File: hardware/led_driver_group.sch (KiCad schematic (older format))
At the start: 26 parts, among them U4 TLC6C5912GQPWRQ1

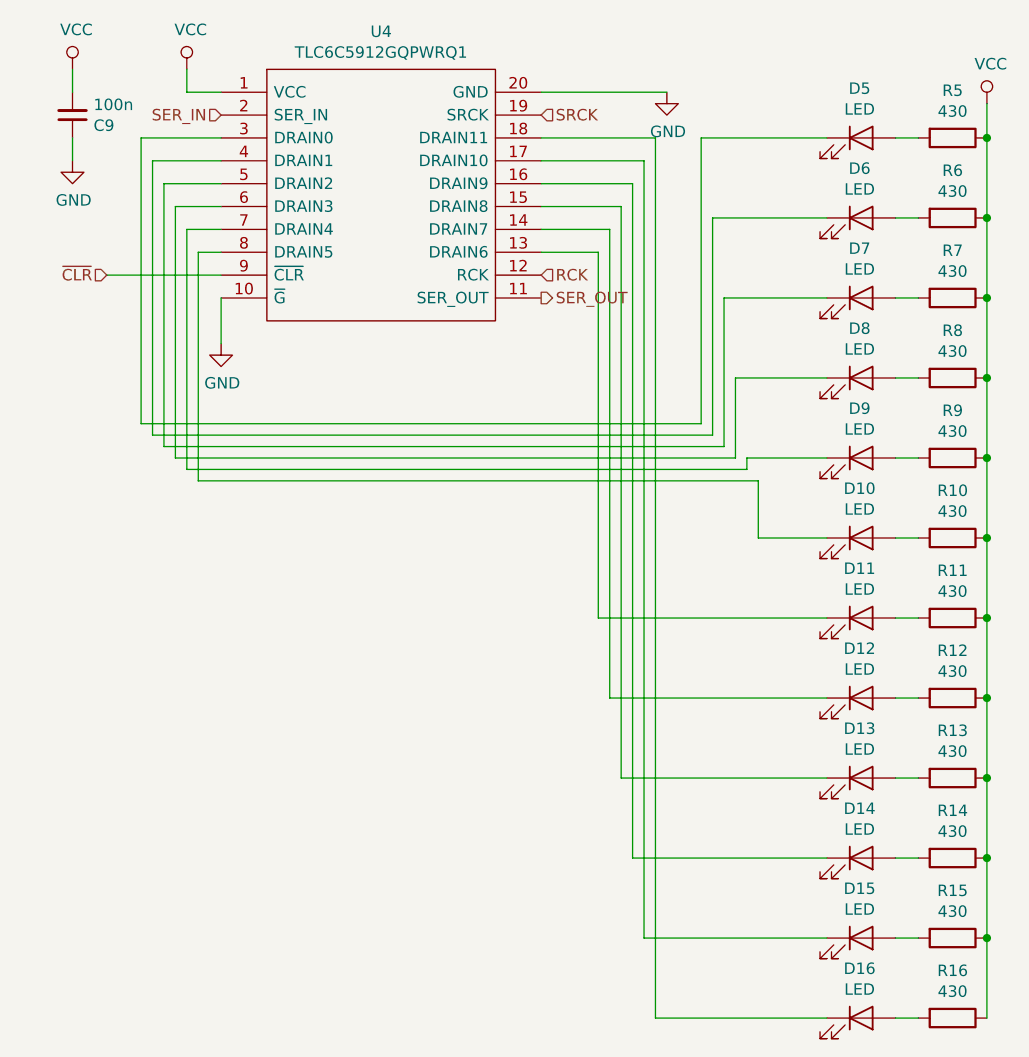
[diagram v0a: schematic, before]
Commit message: Replace J1 with 6 pin connector, use cheaper resistor for 430 ohms.
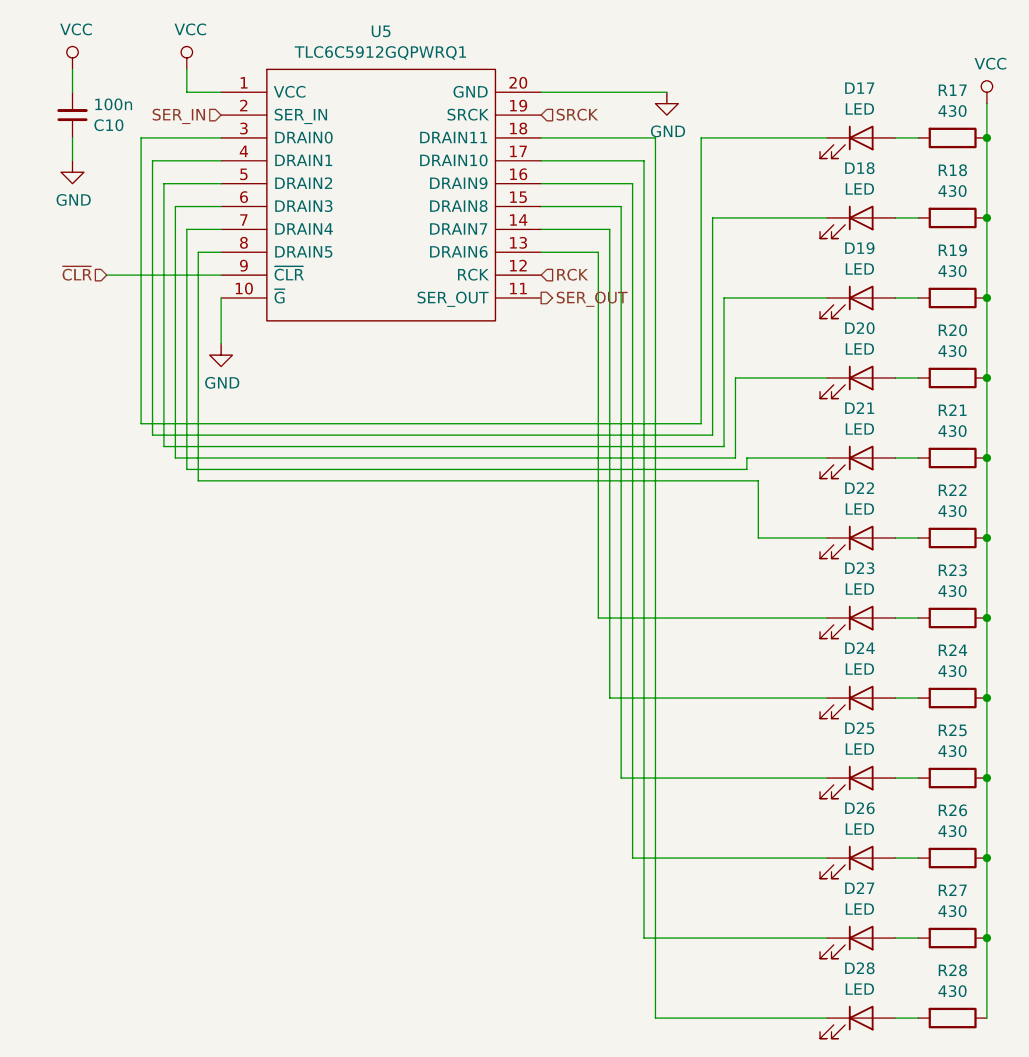
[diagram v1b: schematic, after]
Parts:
- R29, R30, R31, R32, R33, R34, R35, R36, R37, R38, R39, R40: MPN ARG02FTC4300 -> 0402WGF4300TCE; description 430 ±1% 1/16W 0402 High Precision & Low TCR SMD Resistors R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 -> thick film; SMD; 0402; 430Ω; 63mW; ±1%; -55÷155°C
